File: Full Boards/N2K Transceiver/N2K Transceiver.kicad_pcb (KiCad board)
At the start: 4 copper layers, 80 x 60 mm, 75 parts, among them J3 JTAG, SW1 SW_MEC_5G, SW2 SW_MEC_5G, SW3 SW_MEC_5G

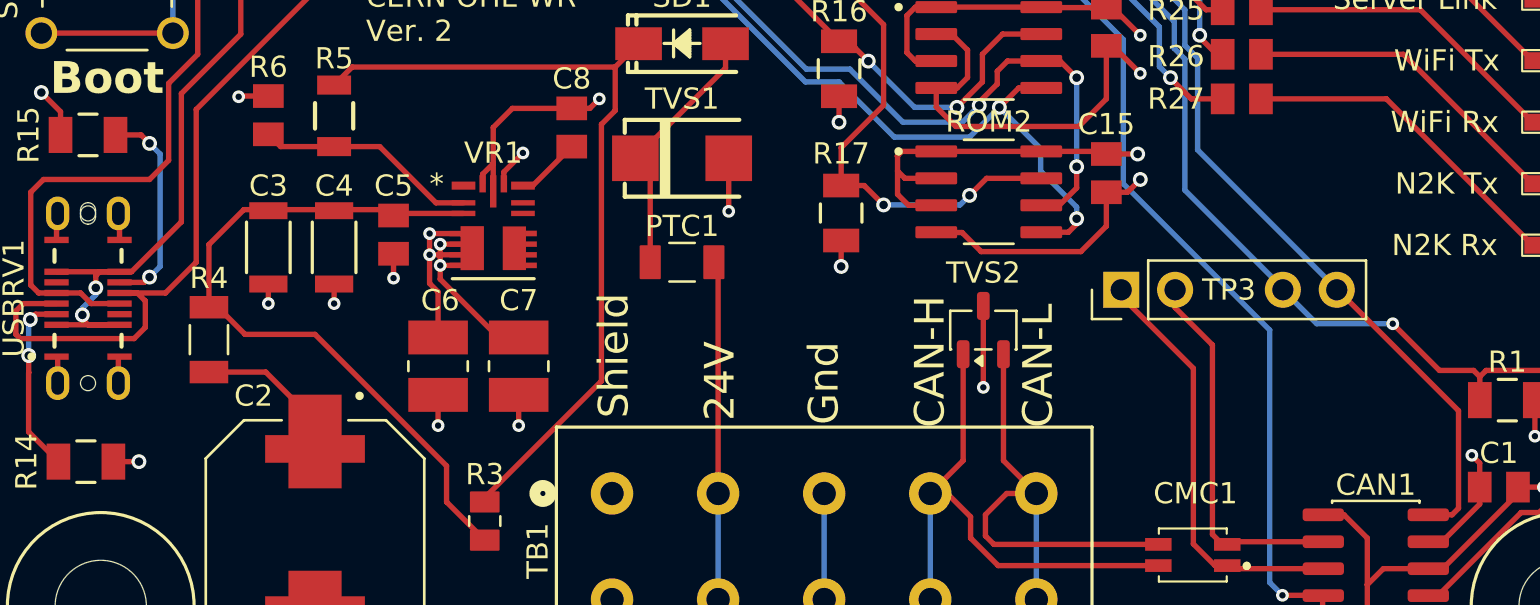
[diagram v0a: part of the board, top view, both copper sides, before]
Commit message: Updated silkscreen.
Signed-off-by: digimer <digital.mermaid@gmail.com>
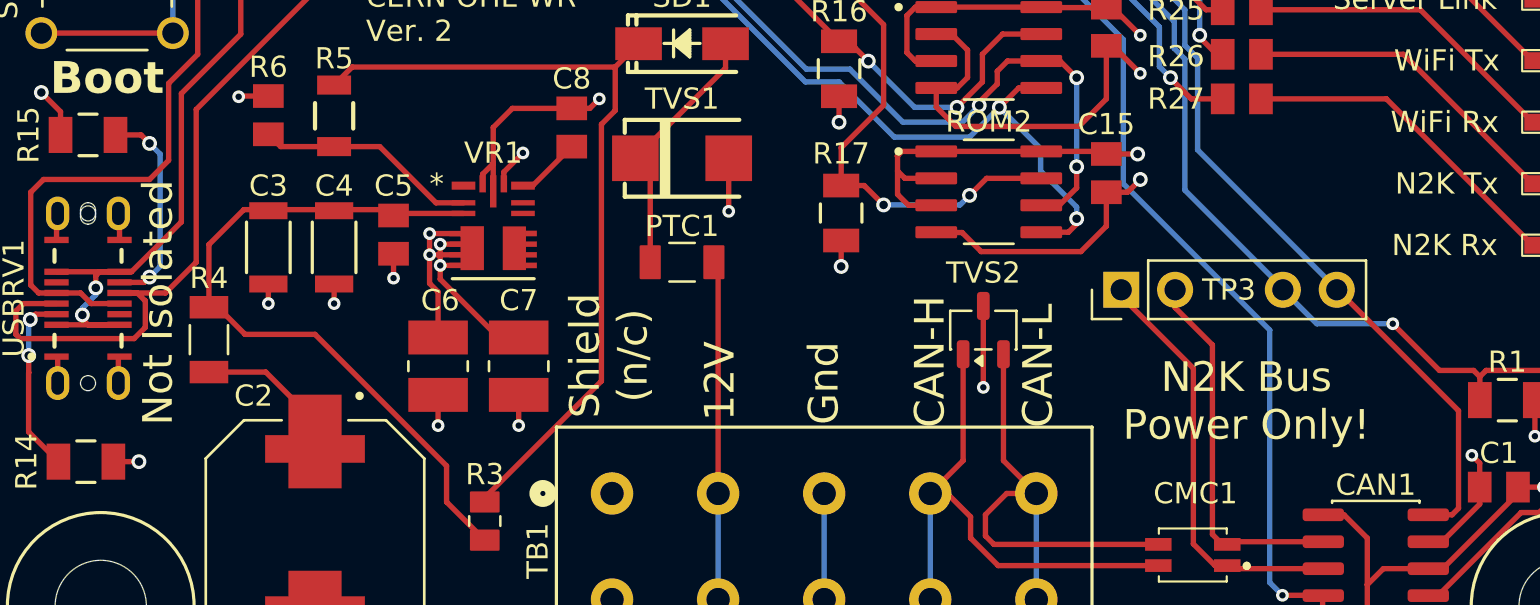
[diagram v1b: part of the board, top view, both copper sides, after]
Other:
- board text added: "12V"
- board text added: "N2K Bus Power Only!"
- board text added: "Not Isolated"
- board text added: "Shield (n/c)"
- board text removed: "24V"
- board text removed: "Shield"
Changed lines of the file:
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@@
 				(type "prepreg")
 				(thickness 0.1)
-				(material "FR4")
+				(material "S1000H")
 				(epsilon_r 4.2)
 				(loss_tangent 0.02)
@@
 				(type "core")
 				(thickness 1.334981)
-				(material "FR4")
+				(material "S1000H")
 				(epsilon_r 4.2)
 				(loss_tangent 0.02)
@@
 				(type "prepreg")
 				(thickness 0.1)
-				(material "FR4")
+				(material "S1000H")
 				(epsilon_r 4.2)
 				(loss_tangent 0.02)
@@
 		)
 	)
+	(gr_text "N2K Bus\nPower Only!"
+		(at 119.5 86.2 0)
+		(layer "F.SilkS")
+		(effects
+			(font
+				(size 1.4 1.4)
+				(thickness 0.2)
+			)
+			(justify top)
+		)
+	)
 	(gr_text "NMEA2000  LEN: 1"
 		(at 99.4 102.7 0)
@@
 		)
 	)
-	(gr_text "Shield"
-		(at 90.5 86 90)
+	(gr_text "Not Isolated"
+		(at 68.2 83.5 90)
+		(layer "F.SilkS")
+		(effects
+			(font
+				(size 1.4 1.4)
+				(thickness 0.2)
+			)
+		)
+	)
+	(gr_text "Shield\n(n/c)"
+		(at 91.4 86 90)
 		(layer "F.SilkS")
 		(effects
@@
 		)
 	)
-	(gr_text "24V"
+	(gr_text "12V"
 		(at 95.5 87.2 90)
 		(layer "F.SilkS")

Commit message: Fixed MTS typo.
Signed-off-by: digimer <digital.mermaid@gmail.com>
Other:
- board text added: "-=] J1 - JTAG 1. GND 2. TMS (MTMS - IO42) 3. TDI (MTDI - IO41) 4. TDO (MTDO - IO40) 5. TCK (MTCK - IO39)"
- board text removed: "-=] J1 - JTAG 1. GND 2. MTS (MTMS - IO42) 3. TDI (MTDI - IO41) 4. TDO (MTDO - IO40) 5. TCK (MTCK - IO39)"
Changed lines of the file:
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@@
 		)
 	)
-	(gr_text "-=] J1 - JTAG\n1. GND\n2. MTS (MTMS - IO42)\n3. TDI (MTDI - IO41)\n4. TDO (MTDO - IO40)\n5. TCK (MTCK - IO39)"
+	(gr_text "-=] J1 - JTAG\n1. GND\n2. TMS (MTMS - IO42)\n3. TDI (MTDI - IO41)\n4. TDO (MTDO - IO40)\n5. TCK (MTCK - IO39)"
 		(at 129.36 51.08 0)
 		(layer "B.SilkS")

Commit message: Fixed T/RXDO->0
Signed-off-by: digimer <digital.mermaid@gmail.com>
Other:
- board text added: "-=] TP1 - MCU 1. +3.3V 2. TXD0 3. RXD0 4. GND"
- board text removed: "-=] TP1 - MCU 1. +3.3V 2. TXDO 3. RXDO 4. GND"
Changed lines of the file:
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@@
 		)
 	)
-	(gr_text "-=] TP1 - MCU\n1. +3.3V\n2. TXDO\n3. RXDO\n4. GND"
+	(gr_text "-=] TP1 - MCU\n1. +3.3V\n2. TXD0\n3. RXD0\n4. GND"
 		(at 114.8 44.1 0)
 		(layer "B.SilkS")

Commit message: Updated PCB to pickup new TP/J annotation.
Signed-off-by: digimer <digital.mermaid@gmail.com>
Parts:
- renumbered J3 to J1, TP3 to TP2
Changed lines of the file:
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@@
 		(descr "Through hole straight pin header, 1x05, 2.54mm pitch, single row")
 		(tags "Through hole pin header THT 1x05 2.54mm single row")
-		(property "Reference" "J3"
+		(property "Reference" "J1"
 			(at 0 -2.38 90)
 			(layer "F.SilkS")
@@
 			(layers "*.Cu" "*.Mask")
 			(remove_unused_layers no)
-			(net "Net-(J3-Pin_2)")
+			(net "Net-(J1-Pin_2)")
 			(pinfunction "Pin_2_2")
 			(pintype "passive")
@@
 			(layers "*.Cu" "*.Mask")
 			(remove_unused_layers no)
-			(net "Net-(J3-Pin_3)")
+			(net "Net-(J1-Pin_3)")
 			(pinfunction "Pin_3_3")
 			(pintype "passive")
@@
 			(layers "*.Cu" "*.Mask")
 			(remove_unused_layers no)
-			(net "Net-(J3-Pin_4)")
+			(net "Net-(J1-Pin_4)")
 			(pinfunction "Pin_4_4")
 			(pintype "passive")
@@
 			(layers "*.Cu" "*.Mask")
 			(remove_unused_layers no)
-			(net "Net-(J3-Pin_5)")
+			(net "Net-(J1-Pin_5)")
 			(pinfunction "Pin_5_5")
 			(pintype "passive")
@@
 			(size 1.5 0.9)
 			(layers "F.Cu" "F.Mask" "F.Paste")
-			(net "Net-(J3-Pin_5)")
+			(net "Net-(J1-Pin_5)")
 			(pinfunction "IO39_32")
 			(pintype "bidirectional")
@@
 			(size 1.5 0.9)
 			(layers "F.Cu" "F.Mask" "F.Paste")
-			(net "Net-(J3-Pin_4)")
+			(net "Net-(J1-Pin_4)")
 			(pinfunction "IO40_33")
 			(pintype "bidirectional")
@@
 			(size 1.5 0.9)
 			(layers "F.Cu" "F.Mask" "F.Paste")
-			(net "Net-(J3-Pin_3)")
+			(net "Net-(J1-Pin_3)")
 			(pinfunction "IO41_34")
 			(pintype "bidirectional")
@@
 			(size 1.5 0.9)
 			(layers "F.Cu" "F.Mask" "F.Paste")
-			(net "Net-(J3-Pin_2)")
+			(net "Net-(J1-Pin_2)")
 			(pinfunction "IO42_35")
 			(pintype "bidirectional")
@@
 		(descr "Through hole straight pin header, 1x05, 2.54mm pitch, single row")
 		(tags "Through hole pin header THT 1x05 2.54mm single row")
-		(property "Reference" "TP3"
+		(property "Reference" "TP2"
 			(at 0 5.08 180)
 			(layer "F.SilkS")
@@
 	)
 	(segment
-		(start 114.4 53.5)
-		(end 120.4 53.5)
-		(width 0.254)
-		(layer "F.Cu")
-		(net "Net-(J3-Pin_2)")
-	)
-	(segment
-		(start 120.4 53.5)
-		(end 120.6 53.3)
-		(width 0.254)
-		(layer "F.Cu")
-		(net "Net-(J3-Pin_2)")
-	)
-	(segment
-		(start 108.75 51.09)
-		(end 111.99 51.09)
-		(width 0.254)
-		(layer "F.Cu")
-		(net "Net-(J3-Pin_2)")
-	)
-	(segment
-		(start 111.99 51.09)
-		(end 114.4 53.5)
-		(width 0.254)
-		(layer "F.Cu")
-		(net "Net-(J3-Pin_2)")
-	)
-	(segment
-		(start 120.6 53.3)
-		(end 120.6 49.34)
-		(width 0.254)
-		(layer "F.Cu")
-		(net "Net-(J3-Pin_2)")
-	)
-	(segment
-		(start 120.6 49.34)
-		(end 120.36 49.1)
-		(width 0.254)
-		(layer "F.Cu")
-		(net "Net-(J3-Pin_2)")
-	)
-	(segment
-		(start 113.8 54.1)
-		(end 120.7 54.1)
-		(width 0.254)
-		(layer "F.Cu")
-		(net "Net-(J3-Pin_3)")
-	)
-	(segment
-		(start 112.06 52.36)
-		(end 113.8 54.1)
-		(width 0.254)
-		(layer "F.Cu")
-		(net "Net-(J3-Pin_3)")
-	)
-	(segment
-		(start 122.9 51.9)
-		(end 122.9 49.1)
-		(width 0.254)
-		(layer "F.Cu")
-		(net "Net-(J3-Pin_3)")
-	)
-	(segment
-		(start 120.7 54.1)
-		(end 122.9 51.9)
-		(width 0.254)
-		(layer "F.Cu")
-		(net "Net-(J3-Pin_3)")
-	)
-	(segment
-		(start 108.75 52.36)
-		(end 112.06 52.36)
-		(width 0.254)
-		(layer "F.Cu")
-		(net "Net-(J3-Pin_3)")
-	)
-	(segment
-		(start 121.2 54.7)
-		(end 125.44 50.46)
-		(width 0.254)
-		(layer "F.Cu")
-		(net "Net-(J3-Pin_4)")
-	)
-	(segment
-		(start 108.75 53.63)
-		(end 111.93 53.63)
-		(width 0.254)
-		(layer "F.Cu")
-		(net "Net-(J3-Pin_4)")
-	)
-	(segment
-		(start 113 54.7)
-		(end 121.2 54.7)
-		(width 0.254)
-		(layer "F.Cu")
-		(net "Net-(J3-Pin_4)")
-	)
-	(segment
-		(start 125.44 50.46)
-		(end 125.44 49.1)
-		(width 0.254)
-		(layer "F.Cu")
-		(net "Net-(J3-Pin_4)")
-	)
-	(segment
-		(start 111.93 53.63)
-		(end 113 54.7)
-		(width 0.254)
-		(layer "F.Cu")
-		(net "Net-(J3-Pin_4)")
-	)
-	(segment
-		(start 111.8 54.9)
-		(end 112.3 55.4)
-		(width 0.254)
-		(layer "F.Cu")
-		(net "Net-(J3-Pin_5)")
-	)
-	(segment
-		(start 112.3 55.4)
-		(end 121.7 55.4)
-		(width 0.254)
-		(layer "F.Cu")
-		(net "Net-(J3-Pin_5)")
-	)
-	(segment
-		(start 127.98 49.12)
-		(end 127.98 49.1)
-		(width 0.254)
-		(layer "F.Cu")
-		(net "Net-(J3-Pin_5)")
-	)
-	(segment
-		(start 108.75 54.9)
-		(end 111.8 54.9)
-		(width 0.254)
-		(layer "F.Cu")
-		(net "Net-(J3-Pin_5)")
-	)
-	(segment
-		(start 121.7 55.4)
-		(end 127.98 49.12)
-		(width 0.254)
-		(layer "F.Cu")
-		(net "Net-(J3-Pin_5)")
-	)
-	(segment
 		(start 87.0017 49.9983)
 		(end 85.4 51.6)
@@
 		(net "Net-(LED7-A)")
 	)
+	(segment
+		(start 113.8 54.1)
+		(end 120.7 54.1)
+		(width 0.254)
+		(layer "F.Cu")
+		(net "Net-(J1-Pin_3)")
+	)
+	(segment
+		(start 112.06 52.36)
+		(end 113.8 54.1)
+		(width 0.254)
+		(layer "F.Cu")
+		(net "Net-(J1-Pin_3)")
+	)
+	(segment
+		(start 122.9 51.9)
+		(end 122.9 49.1)
+		(width 0.254)
+		(layer "F.Cu")
+		(net "Net-(J1-Pin_3)")
+	)
+	(segment
+		(start 120.7 54.1)
+		(end 122.9 51.9)
+		(width 0.254)
+		(layer "F.Cu")
+		(net "Net-(J1-Pin_3)")
+	)
+	(segment
+		(start 108.75 52.36)
+		(end 112.06 52.36)
+		(width 0.254)
+		(layer "F.Cu")
+		(net "Net-(J1-Pin_3)")
+	)
+	(segment
+		(start 114.4 53.5)
+		(end 120.4 53.5)
+		(width 0.254)
+		(layer "F.Cu")
+		(net "Net-(J1-Pin_2)")
+	)
+	(segment
+		(start 120.4 53.5)
+		(end 120.6 53.3)
+		(width 0.254)
+		(layer "F.Cu")
+		(net "Net-(J1-Pin_2)")
+	)
+	(segment
+		(start 108.75 51.09)
+		(end 111.99 51.09)
+		(width 0.254)
+		(layer "F.Cu")
+		(net "Net-(J1-Pin_2)")
+	)
+	(segment
+		(start 111.99 51.09)
+		(end 114.4 53.5)
+		(width 0.254)
+		(layer "F.Cu")
+		(net "Net-(J1-Pin_2)")
+	)
+	(segment
+		(start 120.6 53.3)
+		(end 120.6 49.34)
+		(width 0.254)
+		(layer "F.Cu")
+		(net "Net-(J1-Pin_2)")
+	)
+	(segment
+		(start 120.6 49.34)
+		(end 120.36 49.1)
+		(width 0.254)
+		(layer "F.Cu")
+		(net "Net-(J1-Pin_2)")
+	)
+	(segment
+		(start 121.2 54.7)
+		(end 125.44 50.46)
+		(width 0.254)
+		(layer "F.Cu")
+		(net "Net-(J1-Pin_4)")
+	)
+	(segment
+		(start 108.75 53.63)
+		(end 111.93 53.63)
+		(width 0.254)
+		(layer "F.Cu")
+		(net "Net-(J1-Pin_4)")
+	)
+	(segment
+		(start 113 54.7)
+		(end 121.2 54.7)
+		(width 0.254)
+		(layer "F.Cu")
+		(net "Net-(J1-Pin_4)")
+	)
+	(segment
+		(start 125.44 50.46)
+		(end 125.44 49.1)
+		(width 0.254)
+		(layer "F.Cu")
+		(net "Net-(J1-Pin_4)")
+	)
+	(segment
+		(start 111.93 53.63)
+		(end 113 54.7)
+		(width 0.254)
+		(layer "F.Cu")
+		(net "Net-(J1-Pin_4)")
+	)
+	(segment
+		(start 111.8 54.9)
+		(end 112.3 55.4)
+		(width 0.254)
+		(layer "F.Cu")
+		(net "Net-(J1-Pin_5)")
+	)
+	(segment
+		(start 112.3 55.4)
+		(end 121.7 55.4)
+		(width 0.254)
+		(layer "F.Cu")
+		(net "Net-(J1-Pin_5)")
+	)
+	(segment
+		(start 127.98 49.12)
+		(end 127.98 49.1)
+		(width 0.254)
+		(layer "F.Cu")
+		(net "Net-(J1-Pin_5)")
+	)
+	(segment
+		(start 108.75 54.9)
+		(end 111.8 54.9)
+		(width 0.254)
+		(layer "F.Cu")
+		(net "Net-(J1-Pin_5)")
+	)
+	(segment
+		(start 121.7 55.4)
+		(end 127.98 49.12)
+		(width 0.254)
+		(layer "F.Cu")
+		(net "Net-(J1-Pin_5)")
+	)
 	(zone

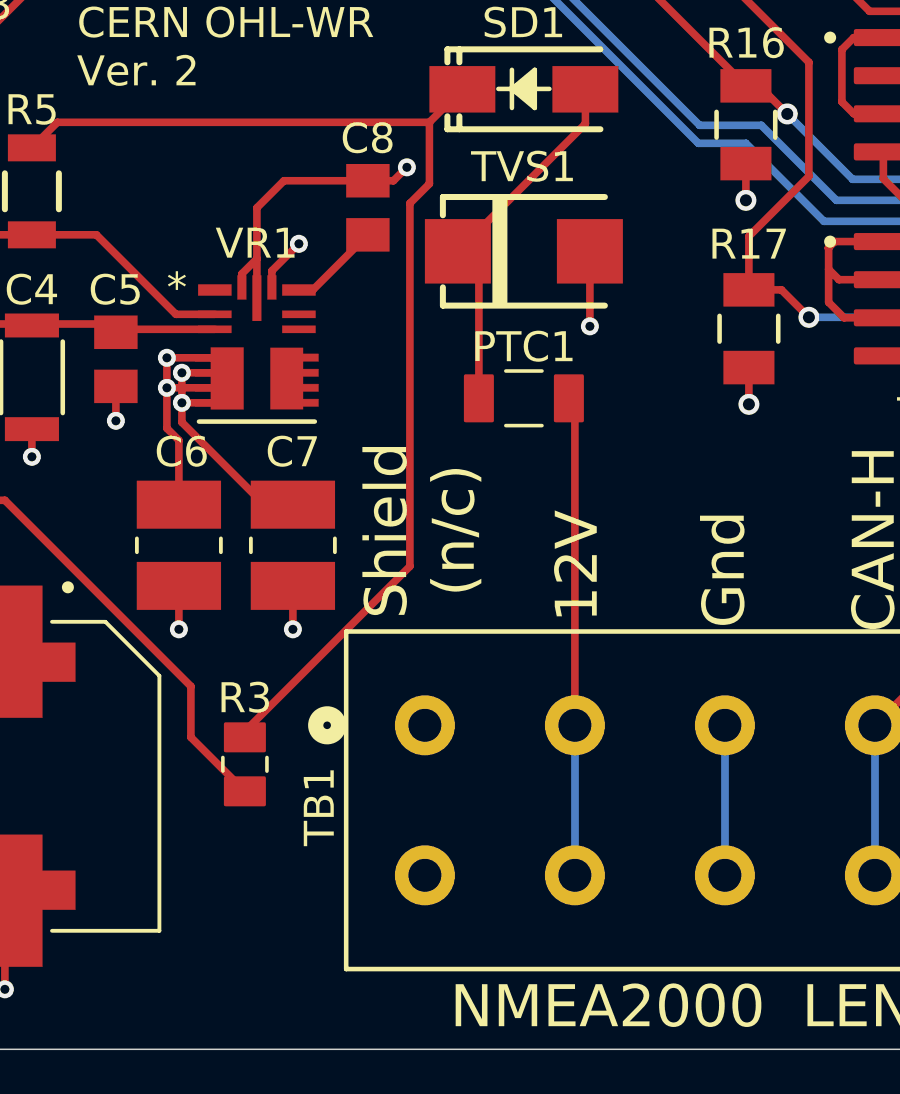
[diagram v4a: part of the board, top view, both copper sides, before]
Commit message: Beefed up the traces from the terminal block to the TVS diode and back to ground to improve transient survival.
Signed-off-by: digimer <digital.mermaid@gmail.com>
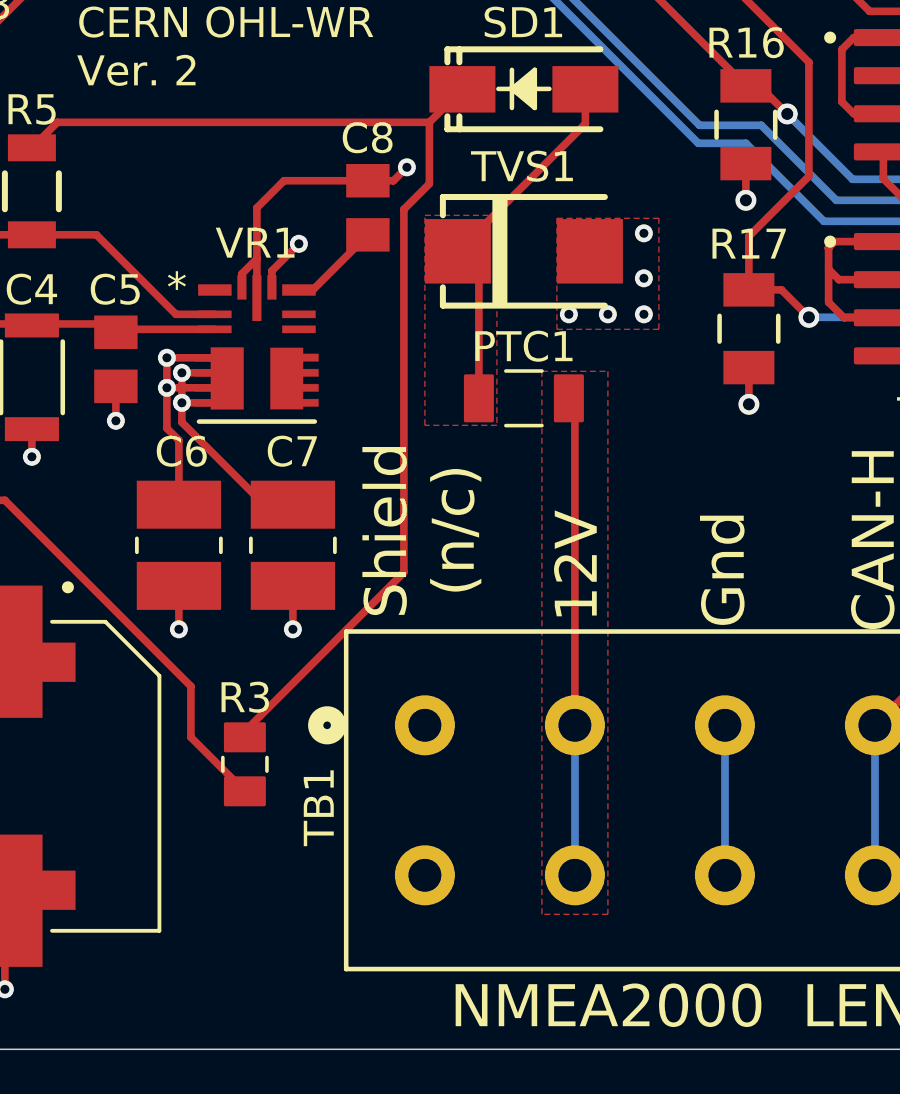
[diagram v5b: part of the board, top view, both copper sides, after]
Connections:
- C1 pad 2: +3.3V -> GND
- C10 pad 1: +3.3V -> GND
- C11 pad 1: +3.3V -> GND
- C14 pad 2: +3.3V -> GND
- C15 pad 2: +3.3V -> GND
- C6 pad 1: +3.3V -> GND
- C7 pad 1: +3.3V -> GND
- C9 pad 2: +3.3V -> GND
- CAN1 pad 3: +3.3V -> GND
- MCU1 pad 2: +3.3V -> GND
- R1 pad 2: +3.3V -> GND
- R16 pad 1: +3.3V -> GND
- R17 pad 1: +3.3V -> GND
- R18 pad 2: +3.3V -> GND
- R19 pad 2: +3.3V -> GND
- R23 pad 2: +3.3V -> GND
- R7 pad 2: +3.3V -> GND
- R8 pad 2: +3.3V -> GND
- ROM1 pad 1: +3.3V -> GND
- ROM1 pad 3: +3.3V -> GND
- ROM1 pad 8: +3.3V -> GND
- ROM2 pad 1: +3.3V -> GND
- ROM2 pad 2: +3.3V -> GND
- ROM2 pad 3: +3.3V -> GND
- ROM2 pad 8: +3.3V -> GND
- VR1 pad 4: +3.3V -> GND
- VR1 pad 9: +3.3V -> GND
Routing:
- net +3.3V: track 78.5 -> 0.00 mm, vias 16 -> 0
- net GND: track 138.4 -> 214.5 mm, vias 29 -> 49
- added copper zone on F.Cu, net GND
- added copper zone on F.Cu, net Net-(PTC1-Pad2)
- added copper zone on F.Cu, net Net-(SD1-A)
